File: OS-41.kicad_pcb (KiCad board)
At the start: 4 copper layers, 0 parts

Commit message: Progress
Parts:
- added AE1: Antenna, libsos41:ANT-SMD_L10.0-W3.0, F.Cu at (138.3, 82.7)
- added C1: 12pF, Capacitor_SMD:C_0603_1608Metric_Pad1.08x0.95mm_HandSolder, F.Cu at (136.0, 120.1)
- added C10: 22uF, Capacitor_SMD:C_0603_1608Metric_Pad1.08x0.95mm_HandSolder, F.Cu at (144.6, 123.0)
- added C11: 10uF, Capacitor_SMD:C_0603_1608Metric_Pad1.08x0.95mm_HandSolder, F.Cu at (141.1, 118.3)
- added C12: 100nF, Capacitor_SMD:C_0603_1608Metric_Pad1.08x0.95mm_HandSolder, F.Cu at (144.6, 120.1)
- added C13: 1uF, Capacitor_SMD:C_0603_1608Metric_Pad1.08x0.95mm_HandSolder, F.Cu at (144.6, 117.4)
- added C14: 100nF, Capacitor_SMD:C_0603_1608Metric_Pad1.08x0.95mm_HandSolder, F.Cu at (205.2, 131.5)
- added C15: 100nF, Capacitor_SMD:C_0603_1608Metric_Pad1.08x0.95mm_HandSolder, F.Cu at (205.2, 134.0)
- added C16: 100nF, Capacitor_SMD:C_0603_1608Metric_Pad1.08x0.95mm_HandSolder, F.Cu at (205.2, 136.5)
- added C17: 100nF, Capacitor_SMD:C_0603_1608Metric_Pad1.08x0.95mm_HandSolder, F.Cu at (205.2, 139.0)
- added C18: 100nF, Capacitor_SMD:C_0603_1608Metric_Pad1.08x0.95mm_HandSolder, F.Cu at (205.2, 141.5)
- added C19: 100nF, Capacitor_SMD:C_0603_1608Metric_Pad1.08x0.95mm_HandSolder, F.Cu at (205.2, 144.0)
- added C2: 8.2pF, Capacitor_SMD:C_0603_1608Metric_Pad1.08x0.95mm_HandSolder, F.Cu at (136.0, 124.2)
- added C20: 100nF, Capacitor_SMD:C_0603_1608Metric_Pad1.08x0.95mm_HandSolder, F.Cu at (205.2, 146.5)
- added C21: 2.2uF, Capacitor_SMD:C_0603_1608Metric_Pad1.08x0.95mm_HandSolder, F.Cu at (209.6, 124.0)
- added C22: 100nF, Capacitor_SMD:C_0603_1608Metric_Pad1.08x0.95mm_HandSolder, F.Cu at (209.6, 126.5)
- added C23: C, Capacitor_SMD:C_0603_1608Metric_Pad1.08x0.95mm_HandSolder, F.Cu at (209.6, 129.0)
- added C24: C, Capacitor_SMD:C_0603_1608Metric_Pad1.08x0.95mm_HandSolder, F.Cu at (209.6, 131.5)
- added C25: C, Capacitor_SMD:C_0603_1608Metric_Pad1.08x0.95mm_HandSolder, F.Cu at (209.6, 134.0)
- added C26: C, Capacitor_SMD:C_0603_1608Metric_Pad1.08x0.95mm_HandSolder, F.Cu at (209.6, 136.5)
- added C3: 9.1pF, Capacitor_SMD:C_0603_1608Metric_Pad1.08x0.95mm_HandSolder, F.Cu at (140.2, 130.9)
- added C4: 10uF, Capacitor_SMD:C_0603_1608Metric_Pad1.08x0.95mm_HandSolder, F.Cu at (200.8, 131.5)
- added C5: 4.7uF, Capacitor_SMD:C_0603_1608Metric_Pad1.08x0.95mm_HandSolder, F.Cu at (200.8, 134.0)
- added C6: 120pF, Capacitor_SMD:C_0603_1608Metric_Pad1.08x0.95mm_HandSolder, F.Cu at (138.5, 118.5)
- added C7: 100nF, Capacitor_SMD:C_0603_1608Metric_Pad1.08x0.95mm_HandSolder, F.Cu at (200.8, 139.0)
- added C8: 1uF, Capacitor_SMD:C_0603_1608Metric_Pad1.08x0.95mm_HandSolder, F.Cu at (143.5, 112.9)
- added C9: 100nF, Capacitor_SMD:C_0603_1608Metric_Pad1.08x0.95mm_HandSolder, F.Cu at (143.6, 111.2)
- added D1: LED, LED_SMD:LED_0805_2012Metric_Pad1.15x1.40mm_HandSolder, F.Cu at (210.4, 149.3)
- added D2: LED, LED_SMD:LED_0805_2012Metric_Pad1.15x1.40mm_HandSolder, F.Cu at (210.4, 152.4)
- added D3: LED, LED_SMD:LED_0805_2012Metric_Pad1.15x1.40mm_HandSolder, F.Cu at (210.4, 155.4)
- added J2: Conn_01x02_Pin, Connector_PinHeader_2.54mm:PinHeader_1x02_P2.54mm_Vertical, F.Cu at (148.2, 112.0)
- added J3: Conn_01x02_Pin, Connector_PinHeader_2.54mm:PinHeader_1x02_P2.54mm_Vertical, F.Cu at (145.2, 132.0)
- added J4: Conn_Coaxial, Connector_Coaxial:SMA_Amphenol_901-144_Vertical, F.Cu at (132.6, 129.3)
- added J6: Conn_01x04_Pin, Connector_PinHeader_2.54mm:PinHeader_1x04_P2.54mm_Vertical, F.Cu at (146.8, 107.7)
- added J8: Conn_01x02_Pin, Connector_PinHeader_2.54mm:PinHeader_1x02_P2.54mm_Vertical, F.Cu at (219.6, 117.8)
- added J9: Conn_01x02_Pin, Connector_PinHeader_2.54mm:PinHeader_1x02_P2.54mm_Vertical, F.Cu at (224.2, 117.8)
- added L1: 270nH, Inductor_SMD:L_0603_1608Metric_Pad1.05x0.95mm_HandSolder, F.Cu at (136.0, 117.5)
- added L2: 11nH, Inductor_SMD:L_0603_1608Metric_Pad1.05x0.95mm_HandSolder, F.Cu at (136.0, 121.6)
- added L3: 24nH, Inductor_SMD:L_0603_1608Metric_Pad1.05x0.95mm_HandSolder, F.Cu at (138.5, 121.8)
- added L4: 39nH, Inductor_SMD:L_0603_1608Metric_Pad1.05x0.95mm_HandSolder, F.Cu at (138.5, 125.1)
- added L5: 24nH, Inductor_SMD:L_0603_1608Metric_Pad1.05x0.95mm_HandSolder, F.Cu at (138.5, 128.4)
- added L6: 4.7uH, libsos41:IND-SMD_L3.3-W3.0, F.Cu at (142.1, 126.7)
- added L7: 10uH, Inductor_SMD:L_0603_1608Metric_Pad1.05x0.95mm_HandSolder, F.Cu at (213.9, 126.5)
- added R1: 50, Resistor_SMD:R_0603_1608Metric_Pad0.98x0.95mm_HandSolder, F.Cu at (132.6, 120.1)
- added R10: 1k, Resistor_SMD:R_0603_1608Metric_Pad0.98x0.95mm_HandSolder, F.Cu at (218.2, 126.5)
- added R11: 1k, Resistor_SMD:R_0603_1608Metric_Pad0.98x0.95mm_HandSolder, F.Cu at (218.2, 129.0)
- added R12: 1k, Resistor_SMD:R_0603_1608Metric_Pad0.98x0.95mm_HandSolder, F.Cu at (218.2, 131.5)
- added R13: 10k, Resistor_SMD:R_0603_1608Metric_Pad0.98x0.95mm_HandSolder, F.Cu at (218.2, 134.0)
- added R14: 10k, Resistor_SMD:R_0603_1608Metric_Pad0.98x0.95mm_HandSolder, F.Cu at (218.2, 136.5)
- added R18: 10k, Resistor_SMD:R_0603_1608Metric_Pad0.98x0.95mm_HandSolder, F.Cu at (218.2, 139.0)
- added R2: 10k, Resistor_SMD:R_0603_1608Metric_Pad0.98x0.95mm_HandSolder, F.Cu at (143.0, 98.2)
- added R3: 976k, Resistor_SMD:R_0603_1608Metric_Pad0.98x0.95mm_HandSolder, F.Cu at (147.1, 121.2)
- added R4: 562k, Resistor_SMD:R_0603_1608Metric_Pad0.98x0.95mm_HandSolder, F.Cu at (148.1, 123.8)
- added R5: 10k, Resistor_SMD:R_0603_1608Metric_Pad0.98x0.95mm_HandSolder, F.Cu at (213.9, 139.0)
- added R6: 10k, Resistor_SMD:R_0603_1608Metric_Pad0.98x0.95mm_HandSolder, F.Cu at (213.9, 141.5)
- added R7: 10k, Resistor_SMD:R_0603_1608Metric_Pad0.98x0.95mm_HandSolder, F.Cu at (213.9, 144.0)
- added R8: 4.7k, Resistor_SMD:R_0603_1608Metric_Pad0.98x0.95mm_HandSolder, F.Cu at (213.9, 146.5)
- added R9: 10k, Resistor_SMD:R_0603_1608Metric_Pad0.98x0.95mm_HandSolder, F.Cu at (218.2, 124.0)
- added U2: SI4432-B1-FMR, centdir:QFN50P400X400X90-21N, F.Cu at (139.0, 113.9)
- added U3: MCP1640x-xCHY, Package_TO_SOT_SMD:SOT-23-6, F.Cu at (146.2, 126.7)
- added U4: ATGM336H-5N31, libsos41:GPSM-SMD_ATGM336H-TR, F.Cu at (143.6, 91.3)
- added U5: DS18B20, Package_TO_SOT_THT:TO-92_Inline, F.Cu at (231.7, 152.6)
- added U6: BMP390L, libsos41:LGA-10_L2.0-W2.0-P0.50-TL_BMP390L, F.Cu at (136.6, 98.5)
- added U7: STM32F411CEUx, Package_DFN_QFN:QFN-48-1EP_7x7mm_P0.5mm_EP5.6x5.6mm, F.Cu at (139.7, 105.0)
- added Y1: Crystal_GND24, Crystal:Crystal_SMD_3225-4Pin_3.2x2.5mm, F.Cu at (130.9, 105.2)
- added Y2: Crystal, Crystal:Crystal_SMD_2012-2Pin_2.0x1.2mm_HandSoldering, F.Cu at (238.5, 156.1)
- added Y3: Crystal_GND24, Crystal:Crystal_SMD_3225-4Pin_3.2x2.5mm, F.Cu at (133.2, 114.5)
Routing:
- net GND: track 0.00 -> 99.7 mm, vias 0 -> 21
- net VCC: track 0.00 -> 73.2 mm, vias 0 -> 11
- net BATT: track 0.00 -> 61.3 mm, vias 0 -> 1
- net SDN: track 0.00 -> 17.8 mm, vias 0 -> 2
- net RXD: track 0.00 -> 15.8 mm, vias 0 -> 2
- net TXD: track 0.00 -> 15.1 mm, vias 0 -> 2
- net NIRQ: track 0.00 -> 13.3 mm, vias 0 -> 2
- net SDA: track 0.00 -> 7.52 mm
- net Net-(U2-XOUT): track 0.00 -> 6.77 mm
- net GPS_ANT: track 0.00 -> 6.32 mm
- net Net-(J4-In): track 0.00 -> 5.94 mm
- net SCL: track 0.00 -> 5.79 mm
- net SWCLK: track 0.00 -> 5.75 mm
- net NSEL: track 0.00 -> 5.57 mm
- net Net-(U2-TX): track 0.00 -> 5.14 mm
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- added copper zone on B.Cu, net GND
- added copper zone on F.Cu, net GND
- added copper zone on In1.Cu, net GND
- added copper zone on In2.Cu, net VCC
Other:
- board outline added: 23.1 x 54.5 mm

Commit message: Preliminary board
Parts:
- removed R8: 4.7k, Resistor_SMD:R_0603_1608Metric_Pad0.98x0.95mm_HandSolder
- removed U5: DS18B20, Package_TO_SOT_THT:TO-92_Inline
- added C27: 100nF, Capacitor_SMD:C_0603_1608Metric_Pad1.08x0.95mm_HandSolder, B.Cu at (146.2, 93.1)
- added C28: 10uF, Capacitor_SMD:C_0603_1608Metric_Pad1.08x0.95mm_HandSolder, B.Cu at (148.0, 93.2)
- C14, C15, C16, C17, C18, C19, C20, C21, C4, C7, R18: moved to B.Cu
- Y2: footprint Crystal:Crystal_SMD_2012-2Pin_2.0x1.2mm_HandSoldering -> Crystal:Crystal_SMD_3215-2Pin_3.2x1.5mm
- moved Y2 120.1 mm to (131.9, 100.6), turned to 180 degrees
- moved D1 102.9 mm to (127.8, 87.9), turned to -90 degrees
- moved D2 102.2 mm to (131.1, 87.9), turned to -90 degrees
- moved D3 101.6 mm to (134.4, 87.9), turned to -90 degrees
- moved J9 98.0 mm to (126.9, 106.7)
- moved R10 97.0 mm to (127.8, 91.4), turned to -90 degrees
- moved J8 95.2 mm to (126.8, 96.4)
- moved R11 94.9 mm to (131.1, 91.4), turned to -90 degrees
- moved R18 94.3 mm to (134.0, 96.6)
- moved R5 94.3 mm to (129.6, 96.8), turned to 90 degrees
- moved R12 92.9 mm to (134.4, 91.4), turned to -90 degrees
- moved R13 92.7 mm to (134.2, 94.9), turned to -90 degrees
- moved R7 92.5 mm to (126.9, 112.7), turned to -90 degrees
- moved R14 91.1 mm to (137.4, 94.5), turned to 90 degrees
- moved R6 88.8 mm to (128.3, 118.0), turned to 180 degrees
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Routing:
- net GND: track 99.7 -> 146.0 mm, vias 21 -> 95
- net VCC: track 73.2 -> 108.4 mm, vias 11 -> 19
- net PB2: track 0.00 -> 29.1 mm
- net NRST: track 0.00 -> 27.2 mm
- net LED_ERR: track 0.00 -> 26.7 mm, vias 0 -> 4
- net BATT: track 61.3 -> 38.1 mm, vias 1 -> 2
- net VREF: track 0.00 -> 16.9 mm, vias 0 -> 1
- net BOOT0: track 0.00 -> 16.9 mm
- net RXD: track 15.8 -> 30.8 mm
- net LED_OK: track 0.00 -> 14.7 mm, vias 0 -> 2
- net Net-(U7-VCAP1): track 0.00 -> 9.50 mm, vias 0 -> 1
- net OSC_IN: track 0.47 -> 9.23 mm
- net Net-(U6-SDO): track 0.00 -> 8.49 mm, vias 0 -> 1
- net OSC32_OUT: track 0.00 -> 8.35 mm
- net OSC_OUT: track 0.45 -> 8.51 mm
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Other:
- board size 23.1 x 54.5 mm -> 26.1 x 54.5 mm
- board text added: "DEBUG"
- board text added: "ERR"
- board text added: "OK"
- board text added: "ON"
- board text added: "OS-41 REV. D"
- board text added: "RF OUT"
- board text added: "STM32+GPS+Horus"

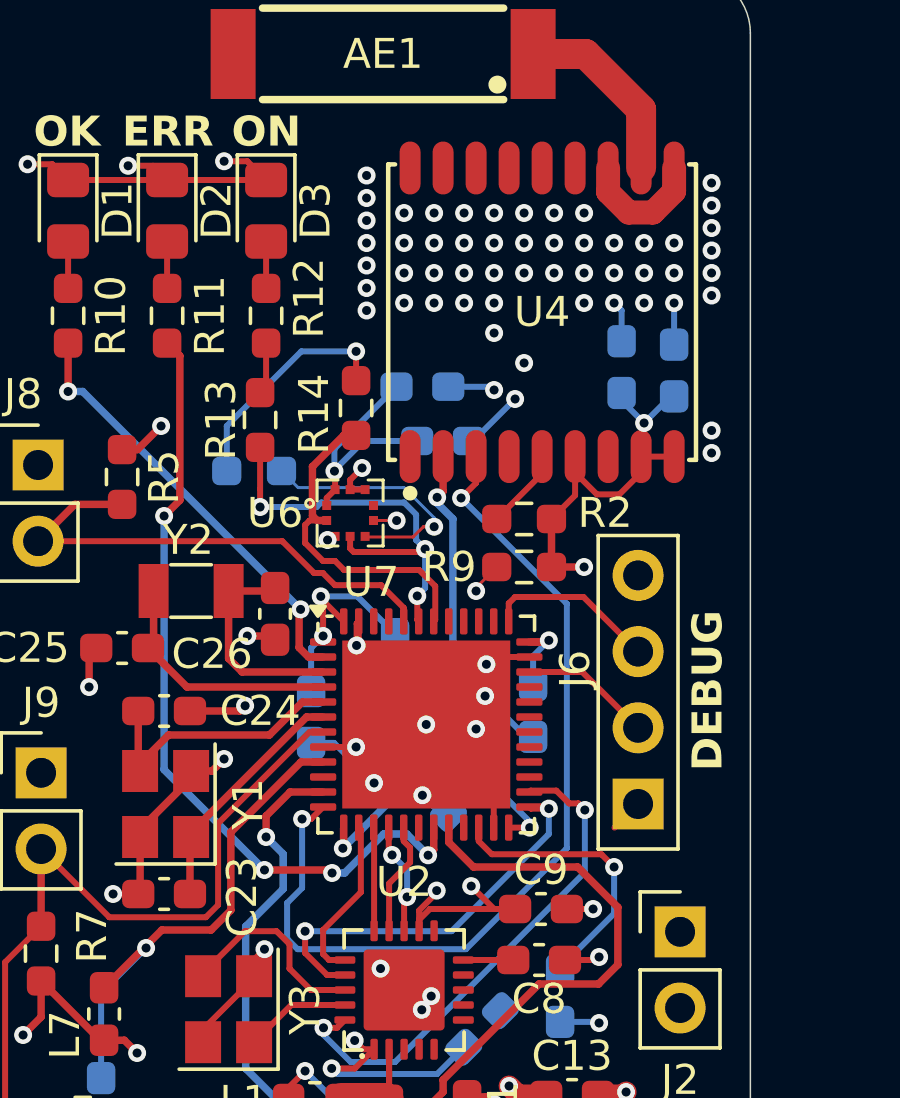
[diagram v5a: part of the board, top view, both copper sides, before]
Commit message: Add 3d models
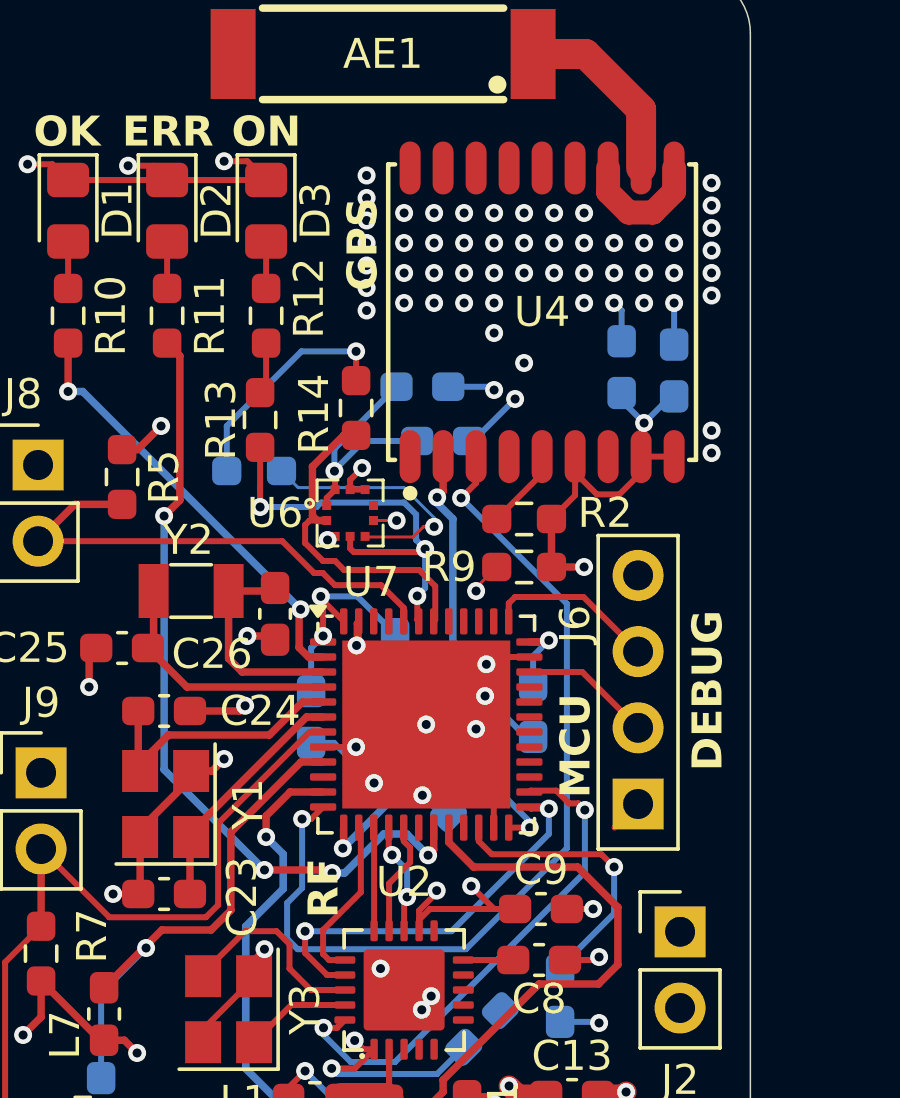
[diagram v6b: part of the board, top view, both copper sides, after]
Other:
- board text added: "CLK"
- board text added: "DIO"
- board text added: "GND"
- board text added: "GPS"
- board text added: "MCU"
- board text added: "RF"
- board text added: "STM32+GPS+Radio"
- board text added: "VCC"
- board text removed: "STM32+GPS+Horus"
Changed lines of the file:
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@@
 				(font
 					(size 0.394101 0.394101)
-					(thickness 0.15)
+					(thickness 0.098525)
 				)
 			)
@@
 			(solder_mask_margin 0.102)
 		)
+		(model "${KIPRJMOD}/Si4432.STEP"
+			(offset
+				(xyz 0 0 0)
+			)
+			(scale
+				(xyz 1 1 1)
+			)
+			(rotate
+				(xyz -90 0 0)
+			)
+		)
 	)
 	(footprint "Resistor_SMD:R_0603_1608Metric_Pad0.98x0.95mm_HandSolder"
@@
 			(pintype "unspecified")
 		)
-		(model "/home/ve3svf/Documents/OS-41/libs.3dshapes/LGA-10_L2.0-W2.0-P0.50-TL_BMP390L.wrl"
+		(model "${KIPRJMOD}/BMP390.STEP"
 			(offset
 				(xyz 0 -0 -0)
@@
 			)
 			(rotate
-				(xyz 0 0 270)
+				(xyz -90 0 0)
 			)
 		)
@@
 			(pintype "passive")
 		)
-		(model "${KICAD8_3DMODEL_DIR}/Connector_Coaxial.3dshapes/SMA_Amphenol_901-144_Vertical.wrl"
+		(model "${KIPRJMOD}/SMA CONNECTOR--3DModel-STEP-1.STEP"
 			(offset
-				(xyz 0 0 0)
+				(xyz 0 0 -4)
 			)
 			(scale
@@
 			)
 			(rotate
-				(xyz 0 0 0)
+				(xyz -90 0 0)
 			)
 		)
@@
 			(pintype "unspecified+no_connect")
 		)
-		(model "${EASYEDA2KICAD}/easyeda2kicad.3dshapes/GPSM-SMD_L10.1-W9.7-H2.4-P1.1.wrl"
+		(model "${KIPRJMOD}/libs.3dshapes/GPSM-SMD_L10.1-W9.7-H2.4-P1.1.step"
 			(offset
 				(xyz 0 -0 -0)
@@
 			(zone_connect 2)
 		)
-		(model "${KICAD8_3DMODEL_DIR}/Package_DFN_QFN.3dshapes/QFN-48-1EP_7x7mm_P0.5mm_EP5.6x5.6mm.wrl"
+		(model "${KIPRJMOD}/STM32.STEP"
 			(offset
 				(xyz 0 0 0)
@@
 			)
 			(rotate
-				(xyz 0 0 0)
+				(xyz -90 0 0)
 			)
 		)
@@
 		(tags "Through hole pin header THT 1x04 2.54mm single row")
 		(property "Reference" "J6"
-			(at 2.1 4.5 -90)
+			(at 2.1 6 -90)
 			(layer "F.SilkS")
 			(effects
@@
 		(tags "capacitor handsolder")
 		(property "Reference" "C4"
-			(at 0 1.43 360)
+			(at 0 1.43 0)
 			(layer "B.SilkS")
 			(effects
@@
 		)
 		(property "Value" "10uF"
-			(at 0 -1.43 360)
+			(at 0 -1.43 0)
 			(layer "B.Fab")
 			(effects
@@
 		)
 		(fp_text user "${REFERENCE}"
-			(at 0 0 360)
+			(at 0 0 0)
 			(layer "B.Fab")
 			(effects
@@
 		(tags "capacitor handsolder")
 		(property "Reference" "C14"
-			(at 0 1.43 360)
+			(at 0 1.43 0)
 			(layer "B.SilkS")
 			(effects
@@
 		)
 		(property "Value" "100nF"
-			(at 0 -1.43 360)
+			(at 0 -1.43 0)
 			(layer "B.Fab")
 			(effects
@@
 		)
 		(fp_text user "${REFERENCE}"
-			(at 0 0 360)
+			(at 0 0 0)
 			(layer "B.Fab")
 			(effects
@@
 		(layer "Edge.Cuts")
 	)
-	(gr_text "STM32+GPS+Horus"
+	(gr_text "STM32+GPS+Radio"
 		(at 145.75 86.5 0)
 		(layer "B.SilkS")
@@
 		)
 	)
+	(gr_text "DIO"
+		(at 148.4 106.6 270)
+		(layer "B.SilkS")
+		(effects
+			(font
+				(size 1 1)
+				(thickness 0.15)
+			)
+			(justify left bottom mirror)
+		)
+	)
+	(gr_text "VCC"
+		(at 148.4 109.9 270)
+		(layer "B.SilkS")
+		(effects
+			(font
+				(size 1 1)
+				(thickness 0.15)
+				(bold yes)
+			)
+			(justify left bottom mirror)
+		)
+	)
 	(gr_text "OS-41 REV. D"
 		(at 146 83.75 -0)
@@
 		)
 	)
+	(gr_text "CLK"
+		(at 148.4 103.8 270)
+		(layer "B.SilkS")
+		(effects
+			(font
+				(size 1 1)
+				(thickness 0.15)
+			)
+			(justify left bottom mirror)
+		)
+	)
+	(gr_text "GND"
+		(at 148.4 100.9 270)
+		(layer "B.SilkS")
+		(effects
+			(font
+				(size 1 1)
+				(thickness 0.15)
+			)
+			(justify left bottom mirror)
+		)
+	)
 	(gr_text "OK"
 		(at 126.65 85.875001 0)
@@
 		)
 	)
+	(gr_text "RF"
+		(at 136.9 111.5 90)
+		(layer "F.SilkS")
+		(effects
+			(font
+				(size 1 1)
+				(thickness 0.2)
+				(bold yes)
+			)
+			(justify left bottom)
+		)
+	)
 	(gr_text "ERR"
 		(at 129.6 85.875001 0)
@@
 		)
 	)
+	(gr_text "MCU"
+		(at 145.3 107.5 90)
+		(layer "F.SilkS")
+		(effects
+			(font
+				(size 1 1)
+				(thickness 0.2)
+				(bold yes)
+			)
+			(justify left bottom)
+		)
+	)
 	(gr_text "ON"
 		(at 133.25 85.875001 0)
 		(layer "F.SilkS")
 		(effects
+			(font
+				(size 1 1)
+				(thickness 0.2)
+				(bold yes)
+			)
+			(justify left bottom)
+		)
+	)
+	(gr_text "GPS"
+		(at 138.2 90.6 90)
+		(layer "F.SilkS")
+		(effects

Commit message: Fix a few more things
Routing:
- net VCC: track 108.4 -> 112.7 mm
- net GND: track 146.0 -> 147.3 mm
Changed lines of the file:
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@@
 	)
 	(segment
+		(start 130.137499 110.7)
+		(end 129.7 110.7)
+		(width 0.25)
+		(layer "F.Cu")
+		(net 3)
+	)
+	(segment
 		(start 130.624999 86.425001)
 		(end 131.1 86.900002)
@@
 	)
 	(segment
+		(start 129.7 110.7)
+		(end 128.6 109.6)
+		(width 0.25)
+		(layer "F.Cu")
+		(net 3)
+	)
+	(segment
 		(start 144.425 111.2)
 		(end 145.3 111.2)
@@
 	)
 	(segment
+		(start 133.2 106.3)
+		(end 132.9 106.6)
+		(width 0.25)
+		(layer "F.Cu")
+		(net 3)
+	)
+	(segment
 		(start 139 113.97)
 		(end 139.59 114.56)
@@
 	)
 	(segment
-		(start 132.6 106.6)
-		(end 133 106.2)
-		(width 0.25)
-		(layer "F.Cu")
-		(net 3)
-	)
-	(segment
 		(start 135.1 126.72)
 		(end 135.1 126.6)
@@
 	)
 	(segment
+		(start 132.9 106.6)
+		(end 131.9 106.6)
+		(width 0.25)
+		(layer "F.Cu")
+		(net 3)
+	)
+	(segment
 		(start 135.175 124.2)
 		(end 134.3 124.2)
@@
 	)
 	(segment
-		(start 130.137499 110.7)
-		(end 129.3 110.7)
-		(width 0.25)
-		(layer "F.Cu")
-		(net 3)
-	)
-	(segment
 		(start 139 113.9)
 		(end 139.699791 113.9)
@@
 	)
 	(segment
-		(start 131.9 106.6)
-		(end 132.6 106.6)
-		(width 0.25)
-		(layer "F.Cu")
-		(net 3)
-	)
-	(segment
 		(start 139.7375 105.05)
 		(end 138.9875 105.8)
@@
 	)
 	(via
-		(at 133 106.2)
+		(at 133.2 106.3)
 		(size 0.6)
 		(drill 0.3)
@@
 	)
 	(via
-		(at 129.3 110.7)
+		(at 128.6 109.6)
 		(size 0.6)
 		(drill 0.3)
@@
 	)
 	(segment
+		(start 137.125001 92.337501)
+		(end 134.4 92.337501)
+		(width 0.2)
+		(layer "F.Cu")
+		(net 6)
+	)
+	(segment
 		(start 147.1 119.6)
 		(end 147.3 119.4)
@@
 	)
 	(segment
+		(start 134.2 92.537501)
+		(end 134.4 92.337501)
+		(width 0.2)
+		(layer "F.Cu")
+		(net 6)
+	)
+	(segment
 		(start 139.5 111.560614)
 		(end 139.5 111.925)
@@
 	)
 	(segment
+		(start 136.9875 101.6125)
+		(end 136.7875 101.6125)
+		(width 0.2)
+		(layer "F.Cu")
+		(net 6)
+	)
+	(segment
 		(start 142 111.2)
 		(end 141.237407 110.437407)
@@
 	)
 	(segment
+		(start 136.7875 101.6125)
+		(end 136.3 102.1)
+		(width 0.2)
+		(layer "F.Cu")
+		(net 6)
+	)
+	(segment
 		(start 145.462501 123)
 		(end 145.462501 120.1375)
@@
 	)
 	(segment
-		(start 134.4 92.337501)
-		(end 134.4 93.7875)
+		(start 137.4 92.6125)
+		(end 137.125001 92.337501)
+		(width 0.2)
+		(layer "F.Cu")
+		(net 6)
+	)
+	(segment
+		(start 134.2 93.9875)
+		(end 134.2 92.537501)
 		(width 0.2)
 		(layer "F.Cu")
@@
 			)
 		)
+	)
+	(zone
+		(net 0)
+		(net_name "")
+		(layers "F.Cu" "In1.Cu" "In2.Cu" "B.Cu")
+		(hatch edge 0.5)
+		(connect_pads
+			(clearance 0)
+		)
+		(min_thickness 0.25)
+		(filled_areas_thickness no)
+		(keepout
+			(tracks allowed)
+			(vias allowed)
+			(pads allowed)
+			(copperpour not_allowed)
+			(footprints allowed)
+		)
+		(fill
+			(thermal_gap 0.5)
+			(thermal_bridge_width 0.5)
+		)
+		(polygon
+			(pts
+				(xy 132.7 104) (xy 132.7 111.3) (xy 129.3 111.3) (xy 129.3 104)
+			)
+		)
